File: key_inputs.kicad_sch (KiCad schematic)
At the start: 41 parts, among them J10 Conn_01x06, J11 Conn_01x16, J12 Conn_01x16, J13 Conn_01x08, J14 Conn_01x08, J6 Conn_01x06, J7 Conn_01x06, J8 Conn_01x06, J9 Conn_01x06

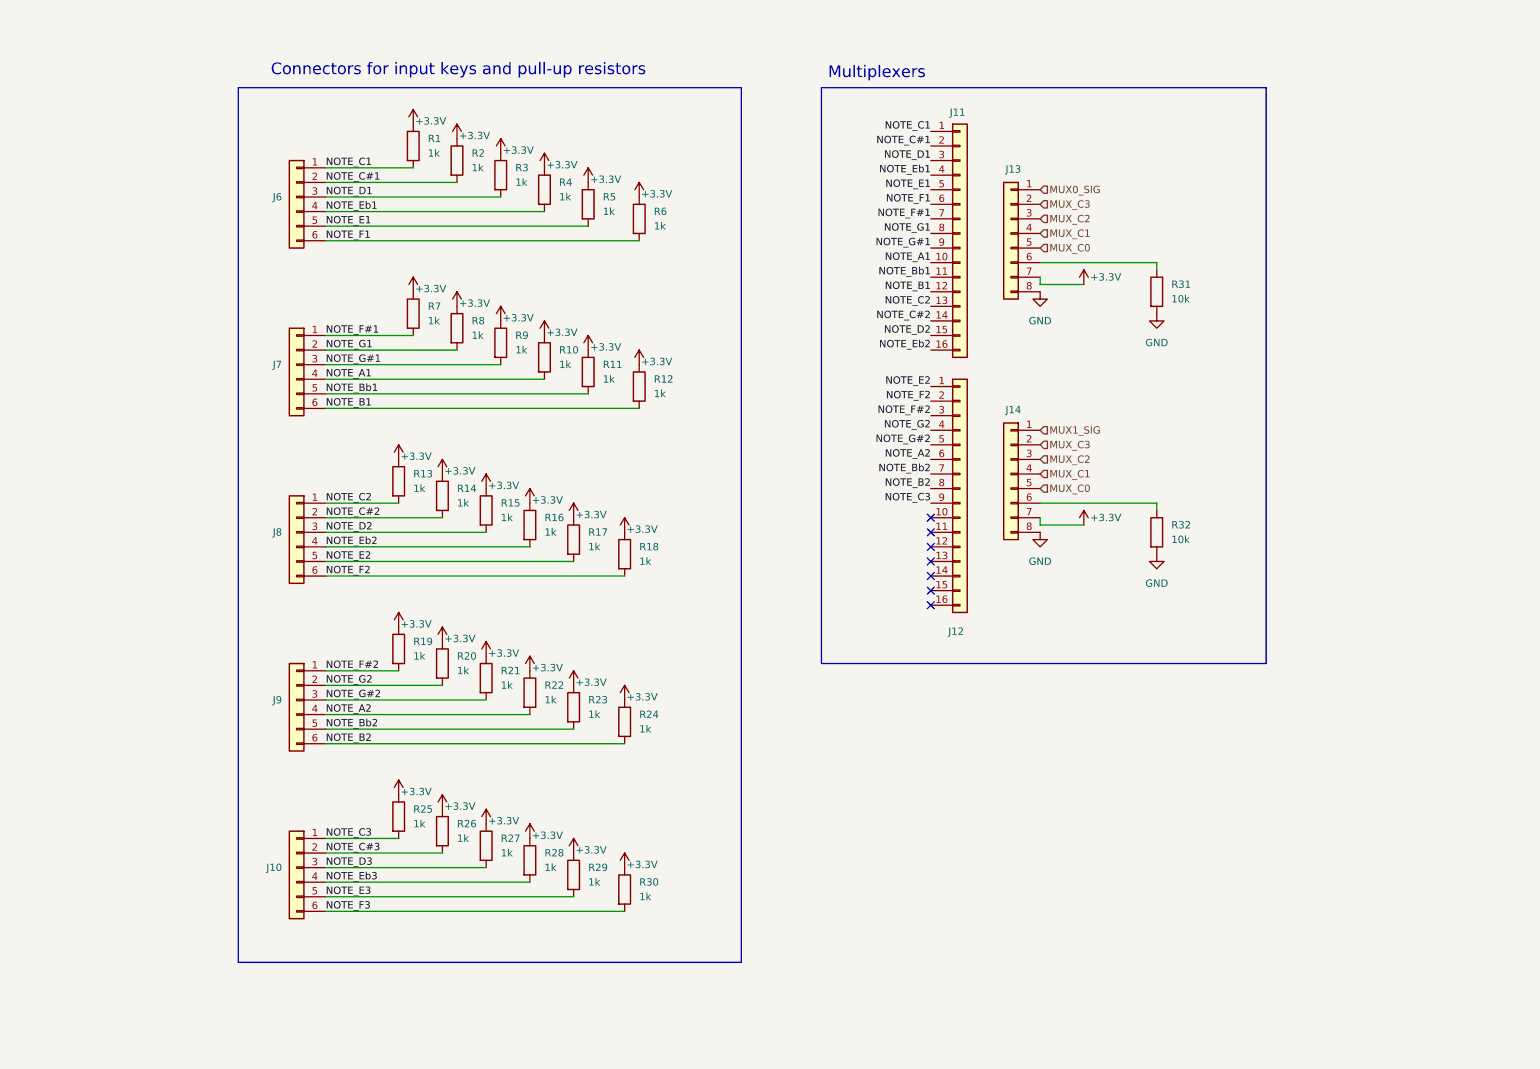
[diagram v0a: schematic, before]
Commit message: fix: replaced 16 channel mux modules with 8 channels mux chips schematic concluded and added 3d models
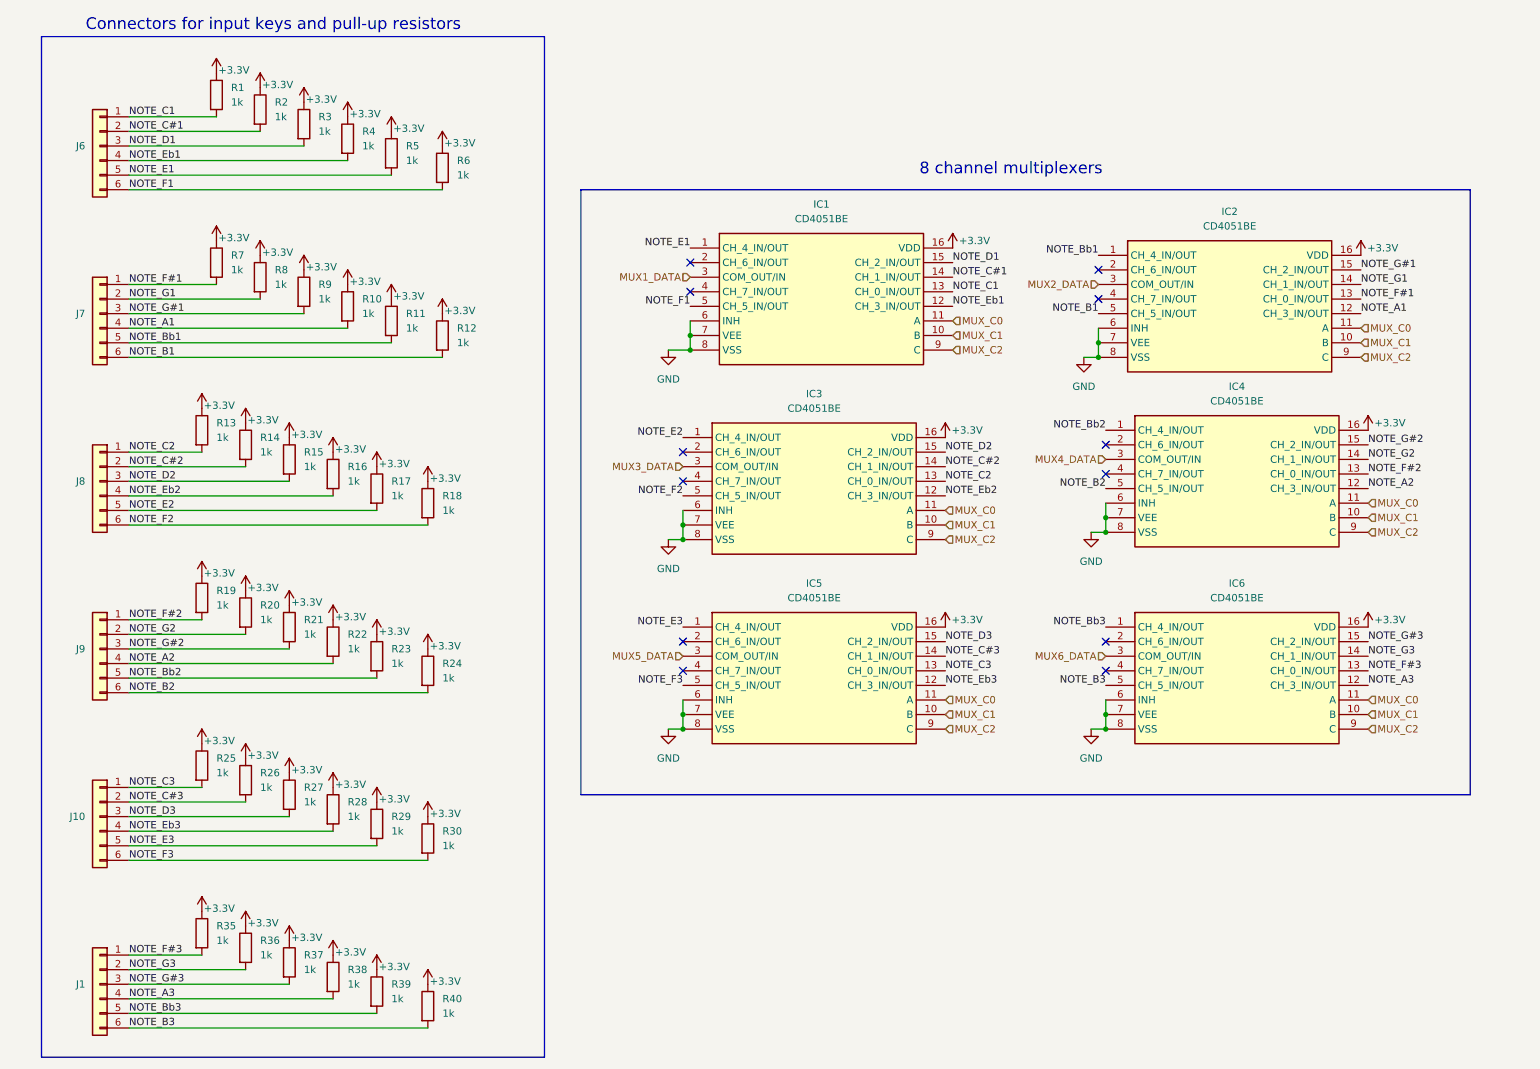
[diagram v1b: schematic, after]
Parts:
- removed J11, J12: Conn_01x16, Connector_PinSocket_2.54mm:PinSocket_1x16_P2.54mm_Vertical, symbol Connector_Generic:Conn_01x16
- removed J13, J14: Conn_01x08, Connector_PinSocket_2.54mm:PinSocket_1x08_P2.54mm_Vertical, symbol Connector_Generic:Conn_01x08
- removed R31, R32: 10k, Resistor_THT:R_Axial_DIN0204_L3.6mm_D1.6mm_P5.08mm_Vertical, symbol Device:R
- added IC1, IC2, IC3, IC4, IC5, IC6: CD4051BE, Library:CD4051BE, symbol CD4051BE:CD4051BE
- added J1: Conn_01x06, Connector_JST:JST_XH_B6B-XH-A_1x06_P2.50mm_Vertical, symbol Connector_Generic:Conn_01x06
- added R35, R36, R37, R38, R39, R40: 1k, Resistor_THT:R_Axial_DIN0204_L3.6mm_D1.6mm_P5.08mm_Vertical, symbol Device:R
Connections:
- net +3.3V: now also IC1.16 (VDD), IC2.16 (VDD), IC3.16 (VDD), IC4.16 (VDD), IC5.16 (VDD), IC6.16 (VDD), R35.1, R36.1, R37.1, R38.1, R39.1, R40.1
- net GND: now also IC1.6 (INH), IC1.7 (VEE), IC1.8 (VSS), IC2.6 (INH), IC2.7 (VEE), IC2.8 (VSS), IC3.6 (INH), IC3.7 (VEE), IC3.8 (VSS), IC4.6 (INH), IC4.7 (VEE), IC4.8 (VSS), IC5.6 (INH), IC5.7 (VEE), IC5.8 (VSS), IC6.6 (INH), IC6.7 (VEE), IC6.8 (VSS)
- net MUX_C0: now also IC1.11 (A), IC2.11 (A), IC3.11 (A), IC4.11 (A), IC5.11 (A), IC6.11 (A)
- net MUX_C1: now also IC1.10 (B), IC2.10 (B), IC3.10 (B), IC4.10 (B), IC5.10 (B), IC6.10 (B)
- net MUX_C2: now also IC1.9 (C), IC2.9 (C), IC3.9 (C), IC4.9 (C), IC5.9 (C), IC6.9 (C)
- net NOTE_A1: now also IC2.12 (CH_3_IN/OUT)
- net NOTE_A2: now also IC4.12 (CH_3_IN/OUT)
- net NOTE_B1: now also IC2.5 (CH_5_IN/OUT)
- net NOTE_B2: now also IC4.5 (CH_5_IN/OUT)
- net NOTE_Bb1: now also IC2.1 (CH_4_IN/OUT)
- net NOTE_Bb2: now also IC4.1 (CH_4_IN/OUT)
- net NOTE_C#1: now also IC1.14 (CH_1_IN/OUT)
- net NOTE_C#2: now also IC3.14 (CH_1_IN/OUT)
- net NOTE_C#3: now also IC5.14 (CH_1_IN/OUT)
- net NOTE_C1: now also IC1.13 (CH_0_IN/OUT)
- net NOTE_C2: now also IC3.13 (CH_0_IN/OUT)
- net NOTE_C3: now also IC5.13 (CH_0_IN/OUT)
- net NOTE_D1: now also IC1.15 (CH_2_IN/OUT)
- net NOTE_D2: now also IC3.15 (CH_2_IN/OUT)
- net NOTE_D3: now also IC5.15 (CH_2_IN/OUT)
- net NOTE_E1: now also IC1.1 (CH_4_IN/OUT)
- net NOTE_E2: now also IC3.1 (CH_4_IN/OUT)
- net NOTE_E3: now also IC5.1 (CH_4_IN/OUT)
- net NOTE_Eb1: now also IC1.12 (CH_3_IN/OUT)
- net NOTE_Eb2: now also IC3.12 (CH_3_IN/OUT)
- net NOTE_Eb3: now also IC5.12 (CH_3_IN/OUT)
- net NOTE_F#1: now also IC2.13 (CH_0_IN/OUT)
- net NOTE_F#2: now also IC4.13 (CH_0_IN/OUT)
- net NOTE_F1: now also IC1.5 (CH_5_IN/OUT)
- net NOTE_F2: now also IC3.5 (CH_5_IN/OUT)
- net NOTE_F3: now also IC5.5 (CH_5_IN/OUT)
- net NOTE_G#1: now also IC2.15 (CH_2_IN/OUT)
- net NOTE_G#2: now also IC4.15 (CH_2_IN/OUT)
- net NOTE_G1: now also IC2.14 (CH_1_IN/OUT)
- net NOTE_G2: now also IC4.14 (CH_1_IN/OUT)
- new net MUX1_DATA: IC1.3 (COM_OUT/IN)
- new net MUX2_DATA: IC2.3 (COM_OUT/IN)
- new net MUX3_DATA: IC3.3 (COM_OUT/IN)
- new net MUX4_DATA: IC4.3 (COM_OUT/IN)
- new net MUX5_DATA: IC5.3 (COM_OUT/IN)
- new net MUX6_DATA: IC6.3 (COM_OUT/IN)
- new net NOTE_A3: IC6.12 (CH_3_IN/OUT), J1.4 (Pin_4), R38.2
- new net NOTE_B3: IC6.5 (CH_5_IN/OUT), J1.6 (Pin_6), R40.2
- new net NOTE_Bb3: IC6.1 (CH_4_IN/OUT), J1.5 (Pin_5), R39.2
- new net NOTE_F#3: IC6.13 (CH_0_IN/OUT), J1.1 (Pin_1), R35.2
- new net NOTE_G#3: IC6.15 (CH_2_IN/OUT), J1.3 (Pin_3), R37.2
- new net NOTE_G3: IC6.14 (CH_1_IN/OUT), J1.2 (Pin_2), R36.2
- no-connect marks 7 -> 12
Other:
- note added: "8 channel multiplexers"
- note removed: "Multiplexers"
- moved on the sheet: J10, J6, J7, J8, J9, R1, R10, R11, R12, R13, R14, R15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

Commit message: layout and routing finished
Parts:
- R1, R10, R11, R12, R13, R14, R15, R16, R17, R18, R19, R2, R20, R21, R22, R23, R24, R25, R26, R27, R28, R29, R3, R30, R35, R36, R37, R38, R39, R4, R40, R5, R6, R7, R8, R9: footprint Resistor_THT:R_Axial_DIN0204_L3.6mm_D1.6mm_P5.08mm_Vertical -> Resistor_THT:R_Axial_DIN0204_L3.6mm_D1.6mm_P5.08mm_Horizontal
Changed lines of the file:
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@@
 			)
 		)
-		(property "Footprint" "Resistor_THT:R_Axial_DIN0204_L3.6mm_D1.6mm_P5.08mm_Vertical"
+		(property "Footprint" "Resistor_THT:R_Axial_DIN0204_L3.6mm_D1.6mm_P5.08mm_Horizontal"
 			(at 70.612 181.61 90)
 			(effects
@@
 			)
 		)
-		(property "Footprint" "Resistor_THT:R_Axial_DIN0204_L3.6mm_D1.6mm_P5.08mm_Vertical"
+		(property "Footprint" "Resistor_THT:R_Axial_DIN0204_L3.6mm_D1.6mm_P5.08mm_Horizontal"
 			(at 87.122 99.06 90)
 			(effects
@@
 			)
 		)
-		(property "Footprint" "Resistor_THT:R_Axial_DIN0204_L3.6mm_D1.6mm_P5.08mm_Vertical"
+		(property "Footprint" "Resistor_THT:R_Axial_DIN0204_L3.6mm_D1.6mm_P5.08mm_Horizontal"
 			(at 78.232 184.15 90)
 			(effects
@@
 			)
 		)
-		(property "Footprint" "Resistor_THT:R_Axial_DIN0204_L3.6mm_D1.6mm_P5.08mm_Vertical"
+		(property "Footprint" "Resistor_THT:R_Axial_DIN0204_L3.6mm_D1.6mm_P5.08mm_Horizontal"
 			(at 62.992 120.65 90)
 			(effects
@@
 			)
 		)
-		(property "Footprint" "Resistor_THT:R_Axial_DIN0204_L3.6mm_D1.6mm_P5.08mm_Vertical"
+		(property "Footprint" "Resistor_THT:R_Axial_DIN0204_L3.6mm_D1.6mm_P5.08mm_Horizontal"
 			(at 70.612 93.98 90)
 			(effects
@@
 			)
 		)
-		(property "Footprint" "Resistor_THT:R_Axial_DIN0204_L3.6mm_D1.6mm_P5.08mm_Vertical"
+		(property "Footprint" "Resistor_THT:R_Axial_DIN0204_L3.6mm_D1.6mm_P5.08mm_Horizontal"
 			(at 55.372 176.53 90)
 			(effects
@@
 			)
 		)
-		(property "Footprint" "Resistor_THT:R_Axial_DIN0204_L3.6mm_D1.6mm_P5.08mm_Vertical"
+		(property "Footprint" "Resistor_THT:R_Axial_DIN0204_L3.6mm_D1.6mm_P5.08mm_Horizontal"
 			(at 47.752 144.78 90)
 			(effects
@@
 			)
 		)
-		(property "Footprint" "Resistor_THT:R_Axial_DIN0204_L3.6mm_D1.6mm_P5.08mm_Vertical"
+		(property "Footprint" "Resistor_THT:R_Axial_DIN0204_L3.6mm_D1.6mm_P5.08mm_Horizontal"
 			(at 55.372 147.32 90)
 			(effects
@@
 			)
 		)
-		(property "Footprint" "Resistor_THT:R_Axial_DIN0204_L3.6mm_D1.6mm_P5.08mm_Vertical"
+		(property "Footprint" "Resistor_THT:R_Axial_DIN0204_L3.6mm_D1.6mm_P5.08mm_Horizontal"
 			(at 70.612 152.4 90)
 			(effects
@@
 			)
 		)
-		(property "Footprint" "Resistor_THT:R_Axial_DIN0204_L3.6mm_D1.6mm_P5.08mm_Vertical"
+		(property "Footprint" "Resistor_THT:R_Axial_DIN0204_L3.6mm_D1.6mm_P5.08mm_Horizontal"
 			(at 47.752 173.99 90)
 			(effects
@@
 			)
 		)
-		(property "Footprint" "Resistor_THT:R_Axial_DIN0204_L3.6mm_D1.6mm_P5.08mm_Vertical"
+		(property "Footprint" "Resistor_THT:R_Axial_DIN0204_L3.6mm_D1.6mm_P5.08mm_Horizontal"
 			(at 80.772 67.31 90)
 			(effects
@@
 			)
 		)
-		(property "Footprint" "Resistor_THT:R_Axial_DIN0204_L3.6mm_D1.6mm_P5.08mm_Vertical"
+		(property "Footprint" "Resistor_THT:R_Axial_DIN0204_L3.6mm_D1.6mm_P5.08mm_Horizontal"
 			(at 73.152 64.77 90)
 			(effects
@@
 			)
 		)
-		(property "Footprint" "Resistor_THT:R_Axial_DIN0204_L3.6mm_D1.6mm_P5.08mm_Vertical"
+		(property "Footprint" "Resistor_THT:R_Axial_DIN0204_L3.6mm_D1.6mm_P5.08mm_Horizontal"
 			(at 87.122 186.69 90)
 			(effects
@@
 			)
 		)
-		(property "Footprint" "Resistor_THT:R_Axial_DIN0204_L3.6mm_D1.6mm_P5.08mm_Vertical"
+		(property "Footprint" "Resistor_THT:R_Axial_DIN0204_L3.6mm_D1.6mm_P5.08mm_Horizontal"
 			(at 70.612 123.19 90)
 			(effects
@@
 			)
 		)
-		(property "Footprint" "Resistor_THT:R_Axial_DIN0204_L3.6mm_D1.6mm_P5.08mm_Vertical"
+		(property "Footprint" "Resistor_THT:R_Axial_DIN0204_L3.6mm_D1.6mm_P5.08mm_Horizontal"
 			(at 78.232 125.73 90)
 			(effects
@@
 			)
 		)
-		(property "Footprint" "Resistor_THT:R_Axial_DIN0204_L3.6mm_D1.6mm_P5.08mm_Vertical"
+		(property "Footprint" "Resistor_THT:R_Axial_DIN0204_L3.6mm_D1.6mm_P5.08mm_Horizontal"
 			(at 62.992 149.86 90)
 			(effects
@@
 			)
 		)
-		(property "Footprint" "Resistor_THT:R_Axial_DIN0204_L3.6mm_D1.6mm_P5.08mm_Vertical"
+		(property "Footprint" "Resistor_THT:R_Axial_DIN0204_L3.6mm_D1.6mm_P5.08mm_Horizontal"
 			(at 50.292 27.94 90)
 			(effects
@@
 			)
 		)
-		(property "Footprint" "Resistor_THT:R_Axial_DIN0204_L3.6mm_D1.6mm_P5.08mm_Vertical"
+		(property "Footprint" "Resistor_THT:R_Axial_DIN0204_L3.6mm_D1.6mm_P5.08mm_Horizontal"
 			(at 89.662 40.64 90)
 			(effects
@@
 			)
 		)
-		(property "Footprint" "Resistor_THT:R_Axial_DIN0204_L3.6mm_D1.6mm_P5.08mm_Vertical"
+		(property "Footprint" "Resistor_THT:R_Axial_DIN0204_L3.6mm_D1.6mm_P5.08mm_Horizontal"
 			(at 87.122 157.48 90)
 			(effects
@@
 			)
 		)
-		(property "Footprint" "Resistor_THT:R_Axial_DIN0204_L3.6mm_D1.6mm_P5.08mm_Vertical"
+		(property "Footprint" "Resistor_THT:R_Axial_DIN0204_L3.6mm_D1.6mm_P5.08mm_Horizontal"
 			(at 55.372 118.11 90)
 			(effects
@@
 			)
 		)
-		(property "Footprint" "Resistor_THT:R_Axial_DIN0204_L3.6mm_D1.6mm_P5.08mm_Vertical"
+		(property "Footprint" "Resistor_THT:R_Axial_DIN0204_L3.6mm_D1.6mm_P5.08mm_Horizontal"
 			(at 50.292 57.15 90)
 			(effects
@@
 			)
 		)
-		(property "Footprint" "Resistor_THT:R_Axial_DIN0204_L3.6mm_D1.6mm_P5.08mm_Vertical"
+		(property "Footprint" "Resistor_THT:R_Axial_DIN0204_L3.6mm_D1.6mm_P5.08mm_Horizontal"
 			(at 57.912 59.69 90)
 			(effects
@@
 			)
 		)
-		(property "Footprint" "Resistor_THT:R_Axial_DIN0204_L3.6mm_D1.6mm_P5.08mm_Vertical"
+		(property "Footprint" "Resistor_THT:R_Axial_DIN0204_L3.6mm_D1.6mm_P5.08mm_Horizontal"
 			(at 78.232 96.52 90)
 			(effects
@@
 			)
 		)
-		(property "Footprint" "Resistor_THT:R_Axial_DIN0204_L3.6mm_D1.6mm_P5.08mm_Vertical"
+		(property "Footprint" "Resistor_THT:R_Axial_DIN0204_L3.6mm_D1.6mm_P5.08mm_Horizontal"
 			(at 62.992 91.44 90)
 			(effects
@@
 			)
 		)
-		(property "Footprint" "Resistor_THT:R_Axial_DIN0204_L3.6mm_D1.6mm_P5.08mm_Vertical"
+		(property "Footprint" "Resistor_THT:R_Axial_DIN0204_L3.6mm_D1.6mm_P5.08mm_Horizontal"
 			(at 62.992 179.07 90)
 			(effects
@@
 			)
 		)
-		(property "Footprint" "Resistor_THT:R_Axial_DIN0204_L3.6mm_D1.6mm_P5.08mm_Vertical"
+		(property "Footprint" "Resistor_THT:R_Axial_DIN0204_L3.6mm_D1.6mm_P5.08mm_Horizontal"
 			(at 87.122 128.27 90)
 			(effects
@@
 			)
 		)
-		(property "Footprint" "Resistor_THT:R_Axial_DIN0204_L3.6mm_D1.6mm_P5.08mm_Vertical"
+		(property "Footprint" "Resistor_THT:R_Axial_DIN0204_L3.6mm_D1.6mm_P5.08mm_Horizontal"
 			(at 89.662 69.85 90)
 			(effects
@@
 			)
 		)
-		(property "Footprint" "Resistor_THT:R_Axial_DIN0204_L3.6mm_D1.6mm_P5.08mm_Vertical"
+		(property "Footprint" "Resistor_THT:R_Axial_DIN0204_L3.6mm_D1.6mm_P5.08mm_Horizontal"
 			(at 57.912 30.48 90)
 			(effects
@@
 			)
 		)
-		(property "Footprint" "Resistor_THT:R_Axial_DIN0204_L3.6mm_D1.6mm_P5.08mm_Vertical"
+		(property "Footprint" "Resistor_THT:R_Axial_DIN0204_L3.6mm_D1.6mm_P5.08mm_Horizontal"
 			(at 55.372 88.9 90)
 			(effects
@@
 			)
 		)
-		(property "Footprint" "Resistor_THT:R_Axial_DIN0204_L3.6mm_D1.6mm_P5.08mm_Vertical"
+		(property "Footprint" "Resistor_THT:R_Axial_DIN0204_L3.6mm_D1.6mm_P5.08mm_Horizontal"
 			(at 47.752 86.36 90)
 			(effects
@@
 			)
 		)
-		(property "Footprint" "Resistor_THT:R_Axial_DIN0204_L3.6mm_D1.6mm_P5.08mm_Vertical"
+		(property "Footprint" "Resistor_THT:R_Axial_DIN0204_L3.6mm_D1.6mm_P5.08mm_Horizontal"
 			(at 65.532 33.02 90)
 			(effects
@@
 			)
 		)
-		(property "Footprint" "Resistor_THT:R_Axial_DIN0204_L3.6mm_D1.6mm_P5.08mm_Vertical"
+		(property "Footprint" "Resistor_THT:R_Axial_DIN0204_L3.6mm_D1.6mm_P5.08mm_Horizontal"
 			(at 80.772 38.1 90)
 			(effects
@@
 			)
 		)
-		(property "Footprint" "Resistor_THT:R_Axial_DIN0204_L3.6mm_D1.6mm_P5.08mm_Vertical"
+		(property "Footprint" "Resistor_THT:R_Axial_DIN0204_L3.6mm_D1.6mm_P5.08mm_Horizontal"
 			(at 73.152 35.56 90)
 			(effects
@@
 			)
 		)
-		(property "Footprint" "Resistor_THT:R_Axial_DIN0204_L3.6mm_D1.6mm_P5.08mm_Vertical"
+		(property "Footprint" "Resistor_THT:R_Axial_DIN0204_L3.6mm_D1.6mm_P5.08mm_Horizontal"
 			(at 65.532 62.23 90)
 			(effects
@@
 			)
 		)
-		(property "Footprint" "Resistor_THT:R_Axial_DIN0204_L3.6mm_D1.6mm_P5.08mm_Vertical"
+		(property "Footprint" "Resistor_THT:R_Axial_DIN0204_L3.6mm_D1.6mm_P5.08mm_Horizontal"
 			(at 78.232 154.94 90)
 			(effects
@@
 			)
 		)
-		(property "Footprint" "Resistor_THT:R_Axial_DIN0204_L3.6mm_D1.6mm_P5.08mm_Vertical"
+		(property "Footprint" "Resistor_THT:R_Axial_DIN0204_L3.6mm_D1.6mm_P5.08mm_Horizontal"
 			(at 47.752 115.57 90)
 			(effects

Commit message: BREAKING: production
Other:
- moved on the sheet: IC1, IC2, IC3, IC4, IC5, IC6
